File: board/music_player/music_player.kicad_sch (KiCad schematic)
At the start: 28 parts, among them J1 Micro_SD_Card_Det1, J2 USB_C_Receptacle_PowerOnly_6P, SW1 SW_SPDT, U1 STM32F401RET6, U2 PCM5102A, Y1 8MHz

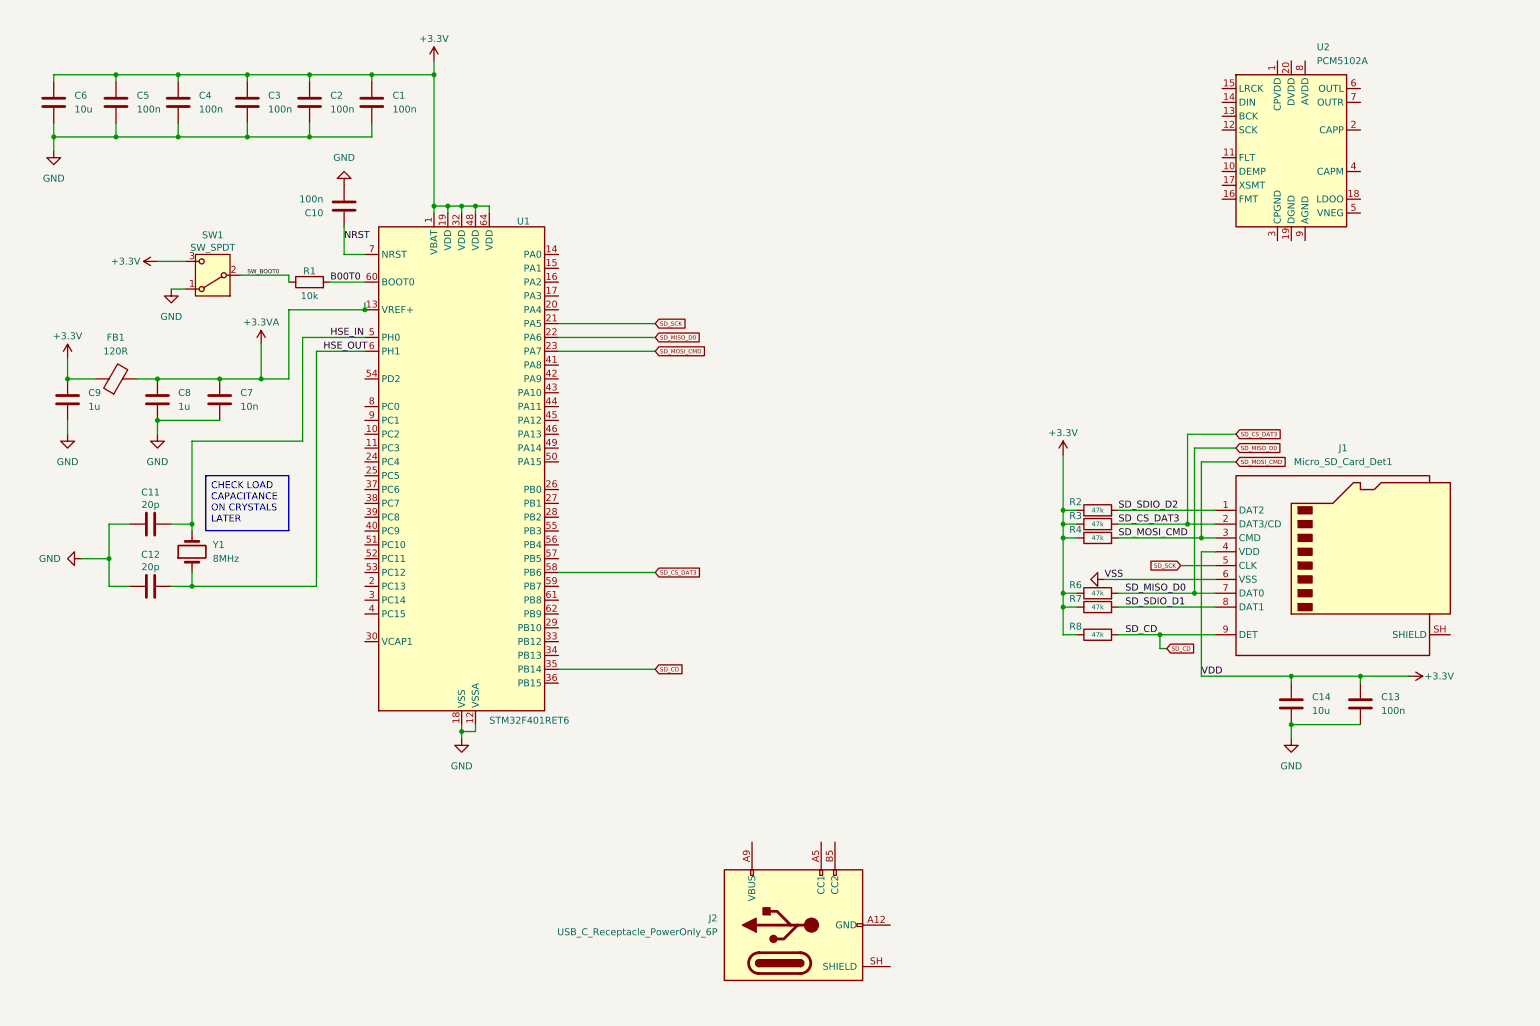
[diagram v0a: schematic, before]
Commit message: update schematic
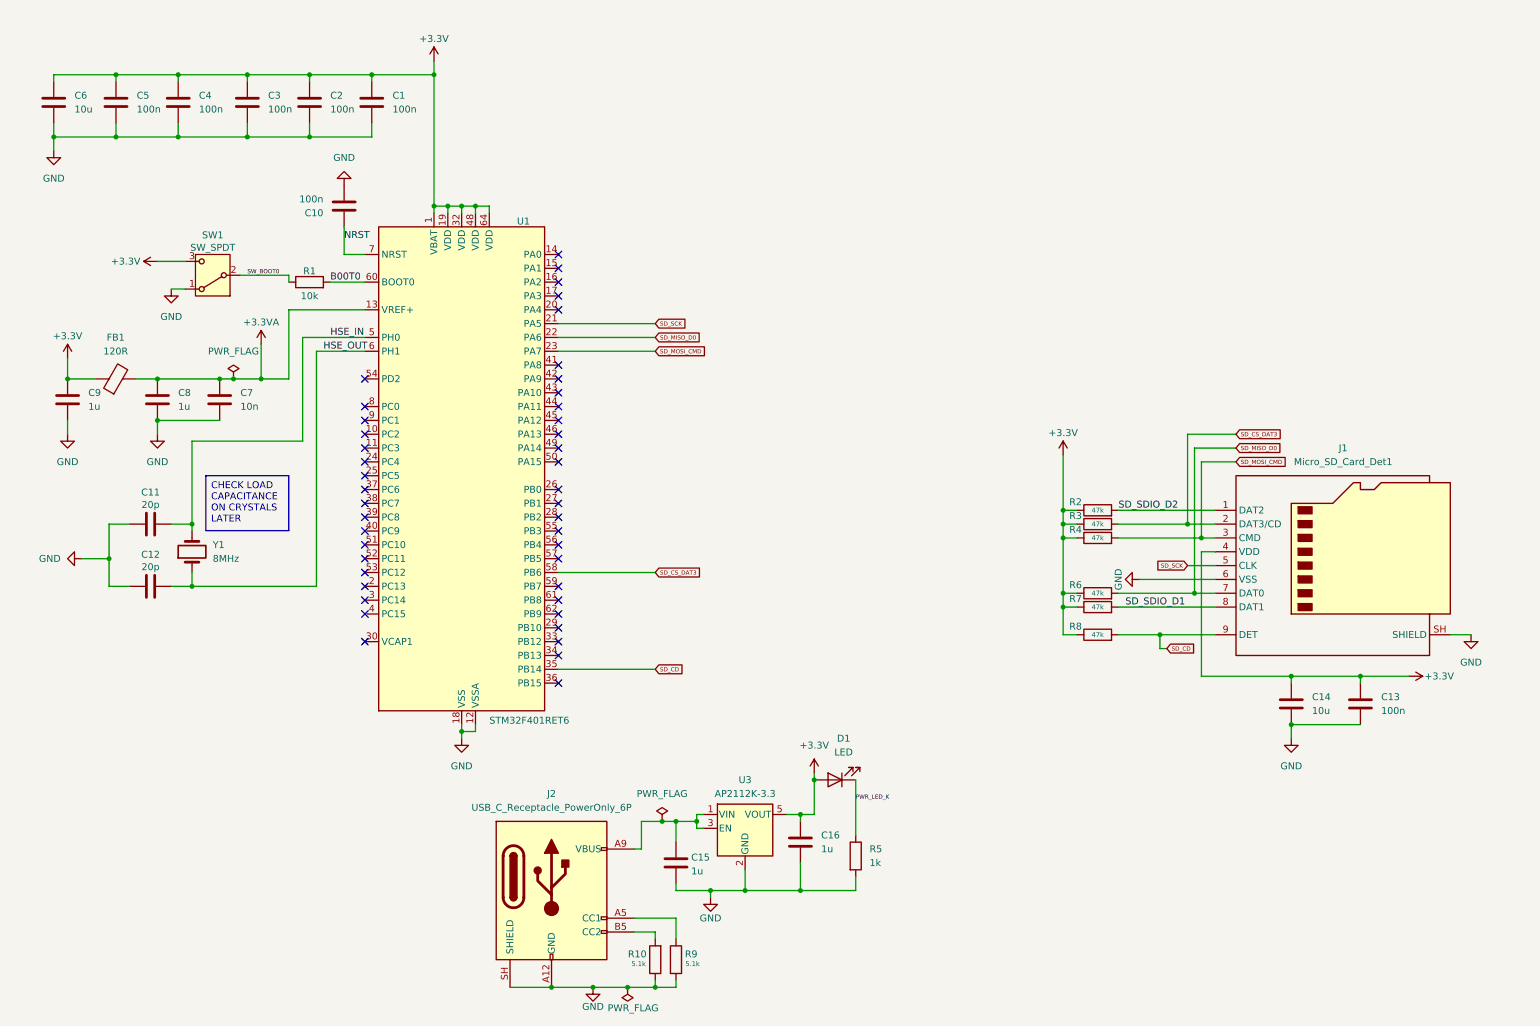
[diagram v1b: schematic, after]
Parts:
- removed U2: PCM5102A, Package_SO:TSSOP-20_4.4x6.5mm_P0.65mm, symbol Audio:PCM5102A
- added C15, C16: 1u, symbol Device:C
- added D1: LED, symbol Device:LED
- added R10, R9: 5.1k, symbol Device:R
- added R5: 1k, symbol Device:R
- added U3: AP2112K-3.3, Package_TO_SOT_SMD:SOT-23-5, symbol Regulator_Linear:AP2112K-3.3
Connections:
- net +3.3V: now also C16.1, D1.2 (A), U3.5 (VOUT)
- net GND: now also J1.SH (SHIELD), J2.A12 (GND), J2.B12 (GND), J2.SH (SHIELD), C15.2, C16.2, R10.1, R5.2, R9.2, U3.2 (GND)
- net at J2.A5 (CC1): now also R9.1
- net at J2.A9 (VBUS), J2.B9 (VBUS): now also C15.1, U3.1 (VIN), U3.3 (EN)
- net at J2.B5 (CC2): now also R10.2
- new net PWR_LED_K: D1.1 (K), R5.1
- no-connect marks 0 -> 44
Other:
- moved on the sheet: J2

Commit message: update schematic
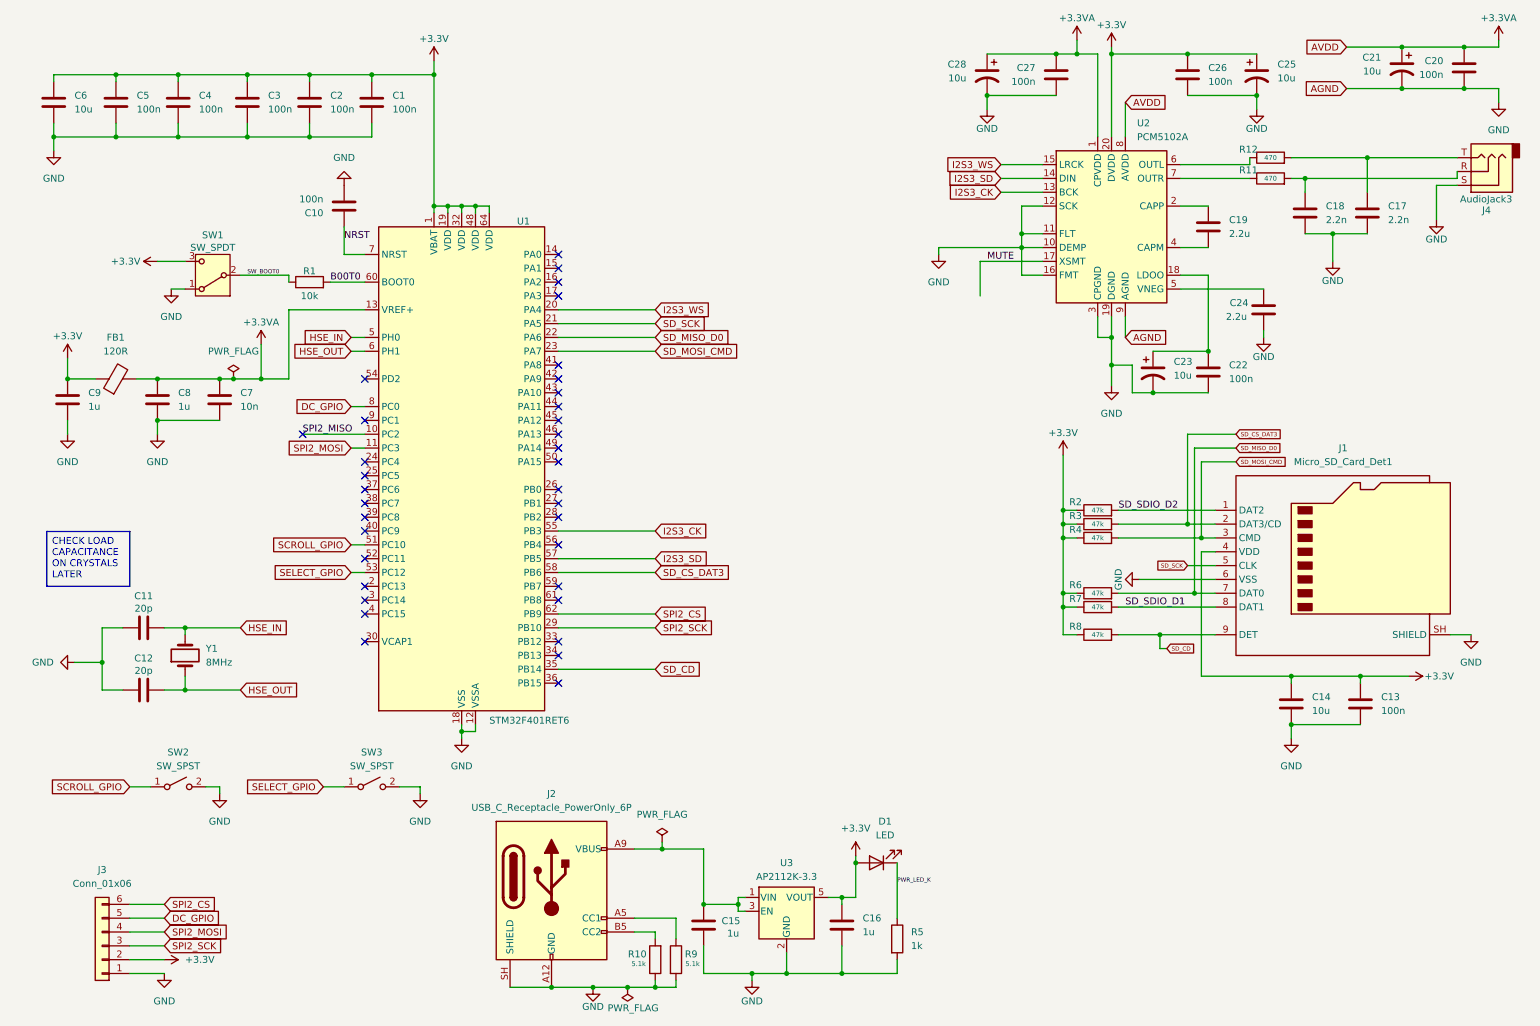
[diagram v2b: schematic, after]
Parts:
- added C17, C18: 2.2n, symbol Device:C
- added C19, C24: 2.2u, symbol Device:C
- added C20, C22, C26, C27: 100n, symbol Device:C
- added C21, C23, C25, C28: 10u, symbol Device:C_Polarized_US
- added J3: Conn_01x06, symbol Connector_Generic:Conn_01x06
- added J4: AudioJack3, symbol Connector_Audio:AudioJack3
- added R11, R12: 470, symbol Device:R
- added SW2, SW3: SW_SPST, symbol Switch:SW_SPST
- added U2: PCM5102A, Package_SO:TSSOP-20_4.4x6.5mm_P0.65mm, symbol Audio:PCM5102A
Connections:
- net +3.3V: now also C25.1, C26.1, J3.2 (Pin_2), U2.20 (DVDD)
- net +3.3VA: now also C20.1, C21.1, C27.1, C28.1, U2.1 (CPVDD), U2.8 (AVDD)
- net GND: now also C17.2, C18.2, C20.2, C21.2, C22.2, C23.2, C24.2, C25.2, C26.2, C27.2, C28.2, J3.1 (Pin_1), J4.S, SW2.2 (B), SW3.2 (B), U2.10 (DEMP), U2.11 (FLT), U2.12 (SCK), U2.16 (FMT), U2.19 (DGND), U2.3 (CPGND), U2.9 (AGND)
- net SPI2_MISO: now reaches U1.10 (PC2)
- net SPI2_MOSI: now reaches U1.11 (PC3)
- net SPI2_MOSI: now also J3.4 (Pin_4)
- net I2S3_WS: now reaches U1.20 (PA4)
- net I2S3_WS: now also U2.15 (LRCK)
- net SPI2_SCK: now reaches U1.29 (PB10)
- net SPI2_SCK: now also J3.3 (Pin_3)
- net SCROLL_GPIO: now reaches U1.51 (PC10)
- net SCROLL_GPIO: now also SW2.1 (A)
- net SELECT_GPIO: now reaches U1.53 (PC12)
- net SELECT_GPIO: now also SW3.1 (A)
- net I2S3_CK: now reaches U1.55 (PB3)
- net I2S3_CK: now also U2.13 (BCK)
- net I2S3_SD: now reaches U1.57 (PB5)
- net I2S3_SD: now also U2.14 (DIN)
- net SPI2_CS: now reaches U1.62 (PB9)
- net SPI2_CS: now also J3.6 (Pin_6)
- net DC_GPIO: now reaches U1.8 (PC0)
- net DC_GPIO: now also J3.5 (Pin_5)
- new net: C22.1, C23.1, U2.18 (LDOO)
- new net: C18.1, J4.R, R11.2
- new net: C17.1, J4.T, R12.2
- new net: C19.1, U2.2 (CAPP)
- new net: C19.2, U2.4 (CAPM)
- new net: R11.1, U2.7 (OUTR)
- new net: C24.1, U2.5 (VNEG)
- new net: R12.1, U2.6 (OUTL)
- new net MUTE: U2.17 (XSMT)
- no-connect marks 44 -> 35
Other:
- moved on the sheet: C11, C12, C15, C16, D1, R5, U3, Y1

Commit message: update schematic
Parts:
- added R13: 10k, symbol Device:R
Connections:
- net MUTE is gone; now on net MUTE_GPIO: U2.17 (XSMT)
- net GND: now also R13.1
- net MUTE_GPIO: now reaches U1.42 (PA9)
- net MUTE_GPIO: now also R13.2
- no-connect marks 35 -> 34
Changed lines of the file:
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@@
 	)
 	(junction
+		(at 185.42 69.85)
+		(diameter 0)
+		(color 0 0 0 0)
+	)
+	(junction
 		(at 143.51 190.5)
 		(diameter 0)
@@
 		(color 0 0 0 0)
 	)
+	(junction
+		(at 182.88 57.15)
+		(diameter 0)
+		(color 0 0 0 0)
+	)
 	(no_connect
 		(at 107.95 83.82)
@@
 	)
 	(no_connect
-		(at 107.95 81.28)
-	)
-	(no_connect
 		(at 107.95 104.14)
 	)
@@
 	(wire
 		(pts
-			(xy 185.42 59.69) (xy 185.42 66.04)
+			(xy 185.42 59.69) (xy 185.42 69.85)
 		)
 		(stroke
@@
 	(wire
 		(pts
+			(xy 182.88 69.85) (xy 185.42 69.85)
+		)
+		(stroke
+			(width 0)
+			(type default)
+		)
+	)
+	(wire
+		(pts
 			(xy 196.85 54.61) (xy 193.04 54.61)
 		)
@@
 	(wire
 		(pts
+			(xy 182.88 57.15) (xy 177.8 57.15)
+		)
+		(stroke
+			(width 0)
+			(type default)
+		)
+	)
+	(wire
+		(pts
 			(xy 186.69 21.59) (xy 199.39 21.59)
 		)
@@
 	(wire
 		(pts
+			(xy 182.88 57.15) (xy 182.88 62.23)
+		)
+		(stroke
+			(width 0)
+			(type default)
+		)
+	)
+	(wire
+		(pts
 			(xy 226.06 135.89) (xy 226.06 113.03)
 		)
@@
 	(wire
 		(pts
+			(xy 185.42 69.85) (xy 185.42 71.12)
+		)
+		(stroke
+			(width 0)
+			(type default)
+		)
+	)
+	(wire
+		(pts
 			(xy 106.68 193.04) (xy 114.3 193.04)
 		)
@@
 	(wire
 		(pts
-			(xy 193.04 57.15) (xy 177.8 57.15)
+			(xy 193.04 57.15) (xy 182.88 57.15)
 		)
 		(stroke
@@
 	(wire
 		(pts
+			(xy 107.95 81.28) (xy 125.73 81.28)
+		)
+		(stroke
+			(width 0)
+			(type default)
+		)
+	)
+	(wire
+		(pts
 			(xy 35.56 138.43) (xy 39.37 138.43)
 		)
@@
 		)
 	)
-	(label "MUTE"
-		(at 186.69 59.69 0)
-		(effects
-			(font
-				(size 1.27 1.27)
-			)
-			(justify left bottom)
-		)
-	)
 	(label "SPI2_MISO"
 		(at 60.96 91.44 0)
@@
 		)
 	)
-	(global_label "AGND"
+	(global_label "AGD"
 		(shape input)
 		(at 252.73 27.94 180)
@@
 		)
 		(property "Intersheetrefs" "${INTERSHEET_REFS}"
-			(at 244.7857 27.94 0)
+			(at 246.1162 27.94 0)
 			(hide yes)
 			(show_name no)
@@
 		)
 	)
+	(global_label "MUTE_GPIO"
+		(shape input)
+		(at 185.42 71.12 0)
+		(fields_autoplaced yes)
+		(effects
+			(font
+				(size 1.27 1.27)
+			)
+			(justify left)
+		)
+		(property "Intersheetrefs" "${INTERSHEET_REFS}"
+			(at 198.7466 71.12 0)
+			(hide yes)
+			(show_name no)
+			(do_not_autoplace no)
+			(effects
+				(font
+					(size 1.27 1.27)
+				)
+				(justify left)
+			)
+		)
+	)
 	(global_label "SELECT_GPIO"
 		(shape input)
@@
 		)
 	)
+	(global_label "MUTE_GPIO"
+		(shape input)
+		(at 125.73 81.28 0)
+		(fields_autoplaced yes)
+		(effects
+			(font
+				(size 1.27 1.27)
+			)
+			(justify left)
+		)
+		(property "Intersheetrefs" "${INTERSHEET_REFS}"
+			(at 139.0566 81.28 0)
+			(hide yes)
+			(show_name no)
+			(do_not_autoplace no)
+			(effects
+				(font
+					(size 1.27 1.27)
+				)
+				(justify left)
+			)
+		)
+	)
 	(global_label "HSE_OUT"
 		(shape input)
@@
 		)
 	)
-	(global_label "AVDD"
+	(global_label "APWR"
 		(shape input)
 		(at 212.09 30.48 0)
@@
 		)
 		(property "Intersheetrefs" "${INTERSHEET_REFS}"
-			(at 219.7924 30.48 0)
+			(at 220.1552 30.48 0)
 			(hide yes)
 			(show_name no)
@@
 		)
 	)
-	(global_label "AVDD"
+	(global_label "APWR"
 		(shape input)
 		(at 252.73 20.32 180)
@@
 		)
 		(property "Intersheetrefs" "${INTERSHEET_REFS}"
-			(at 245.0276 20.32 0)
+			(at 244.6648 20.32 0)
 			(hide yes)
 			(show_name no)
@@
 		)
 	)
-	(global_label "AGND"
+	(global_label "AGD"
 		(shape input)
 		(at 212.09 73.66 0)
@@
 		)
 		(property "Intersheetrefs" "${INTERSHEET_REFS}"
-			(at 220.0343 73.66 0)
+			(at 218.7038 73.66 0)
 			(hide yes)
 			(show_name no)
@@
 		(in_pos_files yes)
 		(dnp no)
-		(fields_autoplaced yes)
 		(property "Reference" "#PWR025"
 			(at 177.8 64.77 0)
@@
 		)
 		(property "Value" "GND"
-			(at 177.8 63.5 0)
+			(at 177.546 62.23 0)
 			(show_name no)
 			(do_not_autoplace no)
@@
 					(unit 1)
 				)
+			)
+		)
+	)
+	(symbol
+		(lib_id "Device:R")
+		(at 182.88 66.04 0)
+		(unit 1)
+		(body_style 1)
+		(exclude_from_sim no)
+		(in_bom yes)
+		(on_board yes)
+		(in_pos_files yes)
+		(dnp no)
+		(property "Reference" "R13"
+			(at 177.8 65.278 0)
+			(show_name no)
+			(do_not_autoplace no)
+			(effects
+				(font
+					(size 1.27 1.27)
+				)
+				(justify left)
+			)
+		)
+		(property "Value" "10k"
+			(at 178.054 67.056 0)
+			(show_name no)
+			(do_not_autoplace no)
+			(effects
+				(font
+					(size 1.27 1.27)
+				)
+				(justify left)
+			)
+		)
+		(property "Footprint" ""
+			(at 181.102 66.04 90)
+			(hide yes)
+			(show_name no)
+			(do_not_autoplace no)
+			(effects
+				(font
+					(size 1.27 1.27)
+				)
+			)
+		)
+		(property "Datasheet" ""
+			(at 182.88 66.04 0)
+			(hide yes)
+			(show_name no)
+			(do_not_autoplace no)
+			(effects
+				(font
+					(size 1.27 1.27)
+				)
+			)
+		)
+		(property "Description" "Resistor"
+			(at 182.88 66.04 0)
+			(hide yes)
+			(show_name no)
+			(do_not_autoplace no)
+			(effects
+				(font
+					(size 1.27 1.27)
+				)
+			)
+		)
+		(pin "2"
+		)
+		(pin "1"
+		)
+		(instances
+			(project "music_player"
+				(path "/da5a1e6a-2605-436b-a30c-1027586d5c0a"
+					(reference "R13")
+					(unit 1)
+				)

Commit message: add st link to schematic and cleanup
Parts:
- added J5: Conn_01x05, symbol Connector_Generic:Conn_01x05
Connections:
- net +3.3V: now also J5.1 (Pin_1)
- net GND: now also J5.3 (Pin_3)
- net PIN_SWDIO: now reaches U1.46 (PA13)
- net PIN_SWDIO: now also J5.4 (Pin_4)
- net PIN_SW_CK: now reaches U1.49 (PA14)
- net PIN_SW_CK: now also J5.2 (Pin_2)
- net NRST renamed PIN_NRST
- net PIN_NRST: now also J5.5 (Pin_5)
- no-connect marks 34 -> 32
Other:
- note added: "Crystal"
- note added: "Microcontroller, Decoupling Caps, Boot SW, and Analog Filter"
- note added: "PCM5102A"
- note added: "SD Card"
- note added: "SPI2 Display Connector"
- note added: "SWD/ST-Link"
- note added: "USB + Regulator"
- moved on the sheet: C13, C14, C17, C18, C19, C20, C21, C22, C23, C24, C25, C26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
